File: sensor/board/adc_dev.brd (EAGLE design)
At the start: 53.3 x 53.3 mm, 44 parts, among them Q2 MC-306 32.7680K-A0, U1 FT232RL

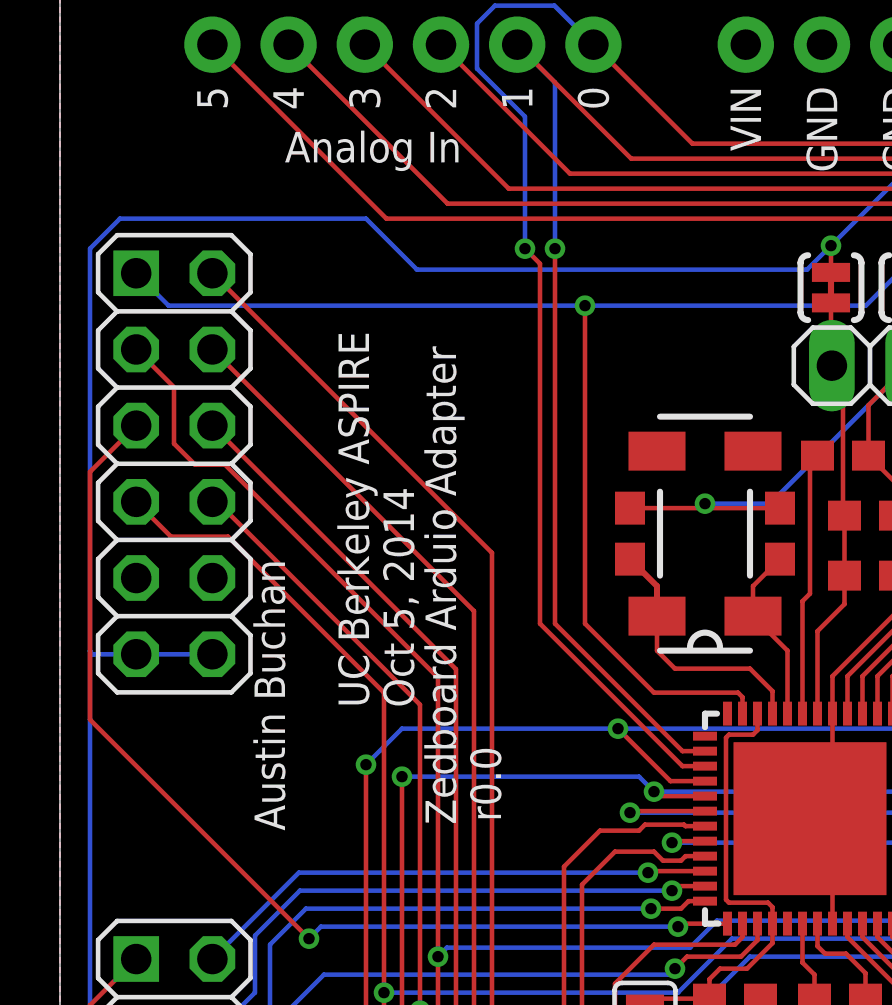
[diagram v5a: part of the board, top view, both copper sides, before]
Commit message: Fixed arduino name
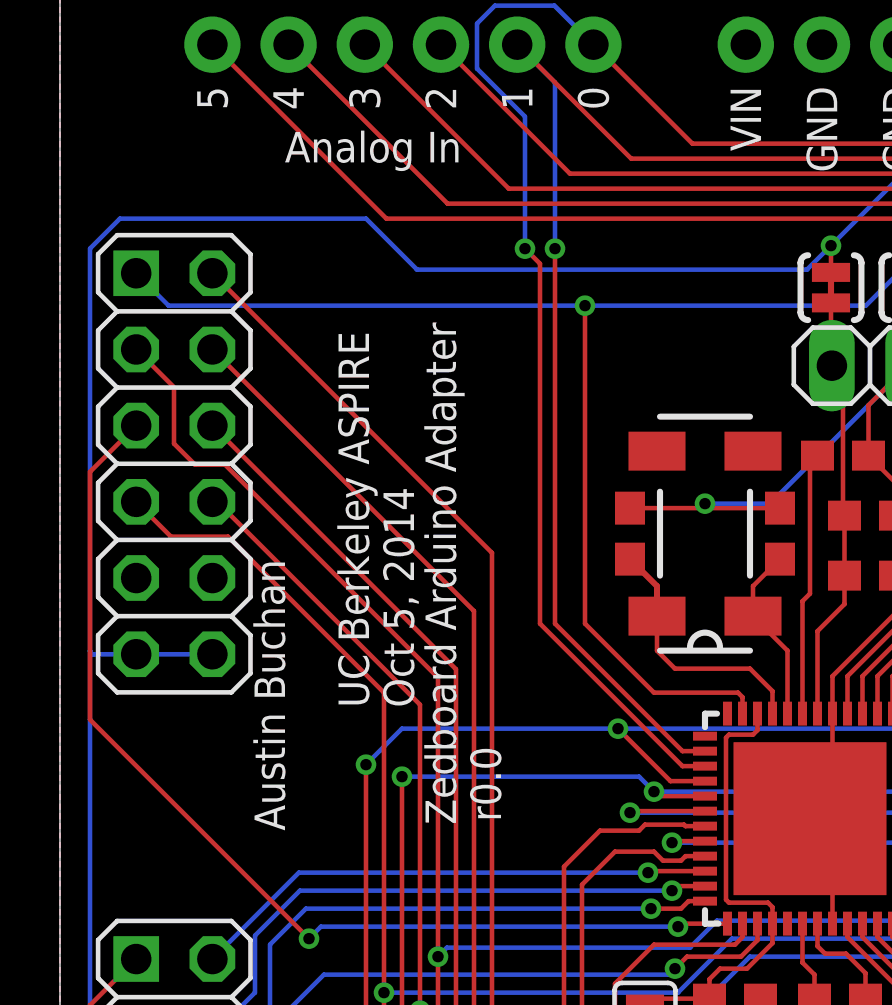
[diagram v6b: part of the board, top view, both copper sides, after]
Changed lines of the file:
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@@
 <layer number="23" name="tOrigins" color="15" fill="1" visible="yes" active="yes"/>
 <layer number="24" name="bOrigins" color="15" fill="1" visible="no" active="yes"/>
-<layer number="25" name="tNames" color="7" fill="1" visible="yes" active="yes"/>
+<layer number="25" name="tNames" color="7" fill="1" visible="no" active="yes"/>
 <layer number="26" name="bNames" color="7" fill="1" visible="no" active="yes"/>
 <layer number="27" name="tValues" color="7" fill="1" visible="yes" active="yes"/>
@@
 <layer number="49" name="Reference" color="7" fill="1" visible="no" active="yes"/>
 <layer number="50" name="dxf" color="7" fill="1" visible="no" active="no"/>
-<layer number="51" name="tDocu" color="7" fill="1" visible="no" active="yes"/>
+<layer number="51" name="tDocu" color="7" fill="1" visible="yes" active="yes"/>
 <layer number="52" name="bDocu" color="7" fill="1" visible="no" active="yes"/>
 <layer number="53" name="tGND_GNDA" color="7" fill="9" visible="no" active="no"/>
@@
 <attribute name="AUTHOR" value="Austin Buchan" x="7.5" y="24.6" size="1.016" layer="21" font="vector" ratio="20" rot="R90"/>
 <attribute name="DATE" value="Oct 5, 2014" x="11.8" y="28.7" size="1.016" layer="21" font="vector" ratio="20" rot="R90"/>
-<attribute name="DESIGN" value="Zedboard Arduio Adapter" x="13.2" y="24.8" size="1.016" layer="21" font="vector" ratio="20" rot="R90"/>
+<attribute name="DESIGN" value="Zedboard Arduino Adapter" x="13.2" y="24.8" size="1.016" layer="21" font="vector" ratio="20" rot="R90"/>
 <attribute name="ORGANIZATION" value="UC Berkeley ASPIRE" x="10.3" y="28.7" size="1.016" layer="21" font="vector" ratio="20" rot="R90"/>
 <attribute name="REVISION" value="r0.0" x="14.7" y="24.9" size="1.016" layer="21" font="vector" ratio="20" rot="R90"/>

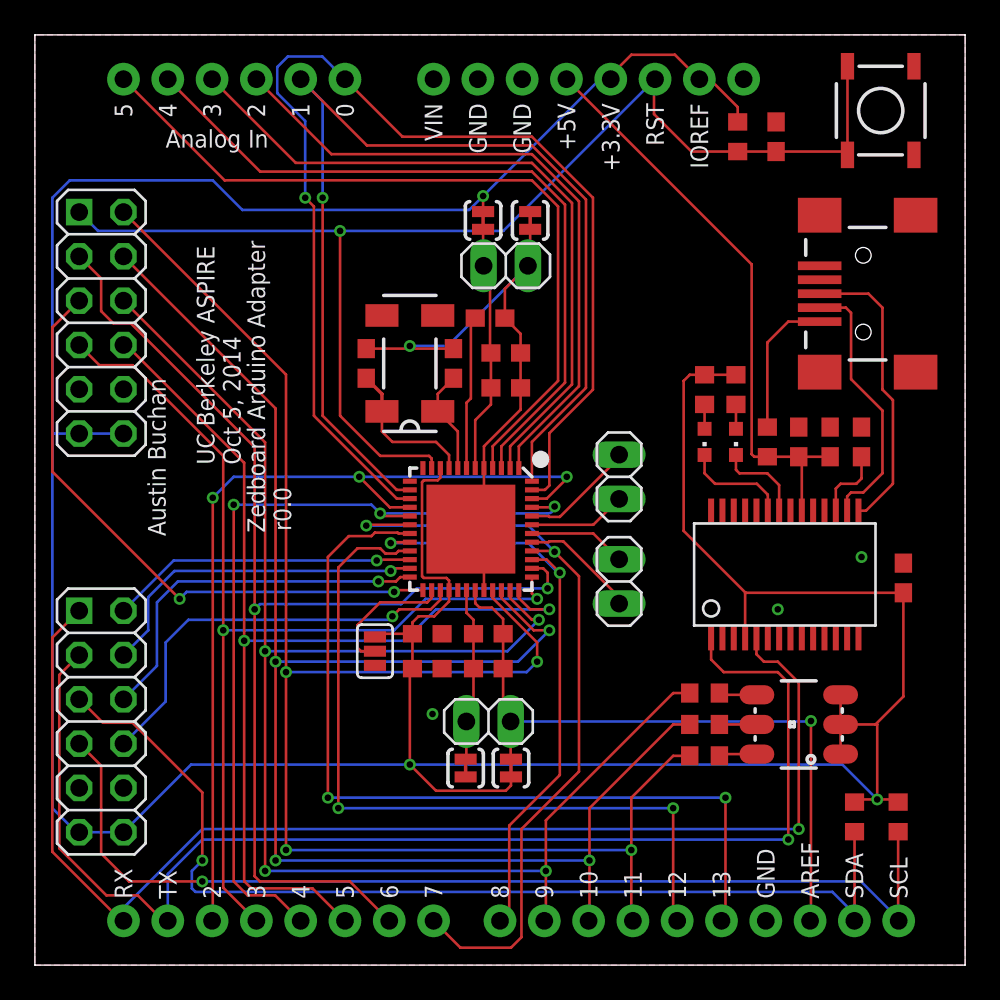
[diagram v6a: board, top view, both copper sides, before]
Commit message: Corrected BLDC mounting holes, added borders to boards, squeezed one more ADC board in to panelization
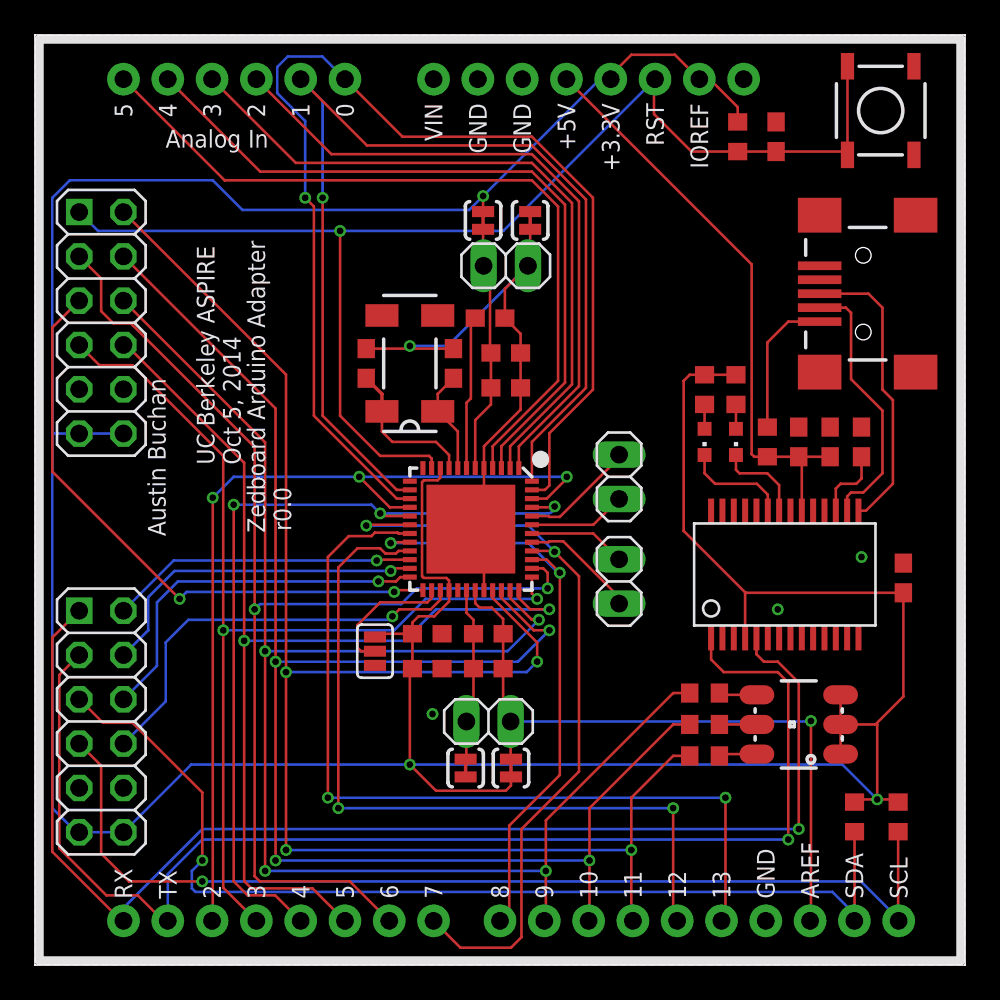
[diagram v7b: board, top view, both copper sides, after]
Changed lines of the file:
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@@
 <setting verticaltext="up"/>
 </settings>
-<grid distance="0.1" unitdist="mm" unit="mm" style="dots" multiple="6" display="yes" altdistance="0.01" altunitdist="mm" altunit="mm"/>
+<grid distance="0.01" unitdist="inch" unit="inch" style="dots" multiple="5" display="yes" altdistance="0.0005" altunitdist="inch" altunit="inch"/>
 <layers>
 <layer number="1" name="Top" color="4" fill="1" visible="yes" active="yes"/>
@@
 <layer number="14" name="Route14" color="1" fill="6" visible="no" active="no"/>
 <layer number="15" name="Route15" color="4" fill="6" visible="no" active="yes"/>
-<layer number="16" name="Bottom" color="1" fill="1" visible="no" active="yes"/>
+<layer number="16" name="Bottom" color="1" fill="1" visible="yes" active="yes"/>
 <layer number="17" name="Pads" color="2" fill="1" visible="yes" active="yes"/>
 <layer number="18" name="Vias" color="2" fill="1" visible="yes" active="yes"/>
@@
 <layer number="20" name="Dimension" color="15" fill="1" visible="yes" active="yes"/>
 <layer number="21" name="tPlace" color="7" fill="1" visible="yes" active="yes"/>
-<layer number="22" name="bPlace" color="7" fill="1" visible="no" active="yes"/>
-<layer number="23" name="tOrigins" color="15" fill="1" visible="yes" active="yes"/>
+<layer number="22" name="bPlace" color="7" fill="1" visible="yes" active="yes"/>
+<layer number="23" name="tOrigins" color="15" fill="1" visible="no" active="yes"/>
 <layer number="24" name="bOrigins" color="15" fill="1" visible="no" active="yes"/>
 <layer number="25" name="tNames" color="7" fill="1" visible="no" active="yes"/>
 <layer number="26" name="bNames" color="7" fill="1" visible="no" active="yes"/>
-<layer number="27" name="tValues" color="7" fill="1" visible="yes" active="yes"/>
+<layer number="27" name="tValues" color="7" fill="1" visible="no" active="yes"/>
 <layer number="28" name="bValues" color="7" fill="1" visible="no" active="yes"/>
-<layer number="29" name="tStop" color="7" fill="3" visible="yes" active="yes"/>
+<layer number="29" name="tStop" color="7" fill="3" visible="no" active="yes"/>
 <layer number="30" name="bStop" color="7" fill="6" visible="no" active="yes"/>
 <layer number="31" name="tCream" color="7" fill="4" visible="no" active="yes"/>
@@
 <layer number="37" name="tTest" color="7" fill="1" visible="no" active="yes"/>
 <layer number="38" name="bTest" color="7" fill="1" visible="no" active="yes"/>
-<layer number="39" name="tKeepout" color="4" fill="11" visible="yes" active="yes"/>
+<layer number="39" name="tKeepout" color="4" fill="11" visible="no" active="yes"/>
 <layer number="40" name="bKeepout" color="1" fill="11" visible="no" active="yes"/>
 <layer number="41" name="tRestrict" color="4" fill="10" visible="no" active="yes"/>
@@
 <layer number="46" name="Milling" color="3" fill="1" visible="no" active="yes"/>
 <layer number="47" name="Measures" color="7" fill="1" visible="no" active="yes"/>
-<layer number="48" name="Document" color="7" fill="1" visible="yes" active="yes"/>
+<layer number="48" name="Document" color="7" fill="1" visible="no" active="yes"/>
 <layer number="49" name="Reference" color="7" fill="1" visible="no" active="yes"/>
 <layer number="50" name="dxf" color="7" fill="1" visible="no" active="no"/>
-<layer number="51" name="tDocu" color="7" fill="1" visible="yes" active="yes"/>
+<layer number="51" name="tDocu" color="7" fill="1" visible="no" active="yes"/>
 <layer number="52" name="bDocu" color="7" fill="1" visible="no" active="yes"/>
 <layer number="53" name="tGND_GNDA" color="7" fill="9" visible="no" active="no"/>
@@
 <text x="19.6" y="12.5" size="1.016" layer="27" font="vector" ratio="25">REFN</text>
 <text x="8.7" y="24.6" size="1.016" layer="27" font="vector" ratio="25" rot="R90">austin.d.buchan@gmail.com</text>
+<wire x1="0.254" y1="0.254" x2="53.086" y2="0.254" width="0.508" layer="21"/>
+<wire x1="53.086" y1="0.254" x2="53.086" y2="53.086" width="0.508" layer="21"/>
+<wire x1="53.086" y1="53.086" x2="0.254" y2="53.086" width="0.508" layer="21"/>
+<wire x1="0.254" y1="53.086" x2="0.254" y2="0.254" width="0.508" layer="21"/>
+<wire x1="0.254" y1="0.254" x2="53.086" y2="0.254" width="0.508" layer="22"/>
+<wire x1="53.086" y1="0.254" x2="53.086" y2="53.086" width="0.508" layer="22"/>
+<wire x1="53.086" y1="53.086" x2="0.254" y2="53.086" width="0.508" layer="22"/>
+<wire x1="0.254" y1="53.086" x2="0.254" y2="0.254" width="0.508" layer="22"/>
 </plain>
 <attributes>

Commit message: Last changes before 2014_11_18 order
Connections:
- net +3V3: no longer SJ1.2, SJ2.2
- net +5V: now also SJ1.2, SJ2.2
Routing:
- net +5V: track 33.6 -> 76.6 mm, vias 0 -> 3
- net +3V3: track 215.8 -> 209.0 mm, vias 3 -> 2
